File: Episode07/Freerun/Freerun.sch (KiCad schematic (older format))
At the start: 17 parts, among them SW1 SW_Push, U1 MAX708, U2 HD6809, Y1 Crystal

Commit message: minor clarification
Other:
- note added: "You can omit the LED and resistor. I add it as\na power indicator, and also a reset indicator\n(the LED turns off when reset is asserted.)\nUsing a high-efficiency LED and limiting the\ncurrent to a few mA is a good idea."
- note removed: "You can omit the LED and resistor. I add it as\na power indicator, and also a reset indicator\n(the LED turns off when reset is asserted.)"
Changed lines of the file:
@@
 Crystal frequency should be between 2 and 4 MHz.\nI used 3.8668 MHz.
 Text Notes 5300 1350 0    50   ~ 0
-You can omit the LED and resistor.  I add it as\na power indicator, and also a reset indicator\n(the LED turns off when reset is asserted.)
+You can omit the LED and resistor.  I add it as\na power indicator, and also a reset indicator\n(the LED turns off when reset is asserted.)\nUsing a high-efficiency LED and limiting the\ncurrent to a few mA is a good idea.
 Text Notes 6400 6950 0    50   ~ 0
 6809 freerun circuit

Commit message: minor fixes
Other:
- note added: "Crystal frequency should be between 2 and 4 MHz.\nI used 3.6864 MHz."
- note removed: "Crystal frequency should be between 2 and 4 MHz.\nI used 3.8668 MHz."
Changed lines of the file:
@@
 EESchema Schematic File Version 4
+LIBS:Freerun-cache
 EELAYER 26 0
 EELAYER END
@@
 	1    0    0    -1
 $EndComp
-Text Notes 6800 6350 0    50   ~ 0
+Text Notes 6800 6600 0    50   ~ 0
 Make all of the pull-up/pull-down resistors connected\nto the data bus (D0..D7) fairly large, e.g., 4.7K.  The\nresistors cause the CPU to read the value 0x12 when\nan instruction is fetched.  0x12 is the opcode of the\nNOP instruction.
 Wire Wire Line
@@
 	3000 3650 3000 3350
 Text Notes 5500 2900 0    50   ~ 0
-Crystal frequency should be between 2 and 4 MHz.\nI used 3.8668 MHz.
+Crystal frequency should be between 2 and 4 MHz.\nI used 3.6864 MHz.
 Text Notes 5300 1350 0    50   ~ 0
 You can omit the LED and resistor.  I add it as\na power indicator, and also a reset indicator\n(the LED turns off when reset is asserted.)\nUsing a high-efficiency LED and limiting the\ncurrent to a few mA is a good idea.

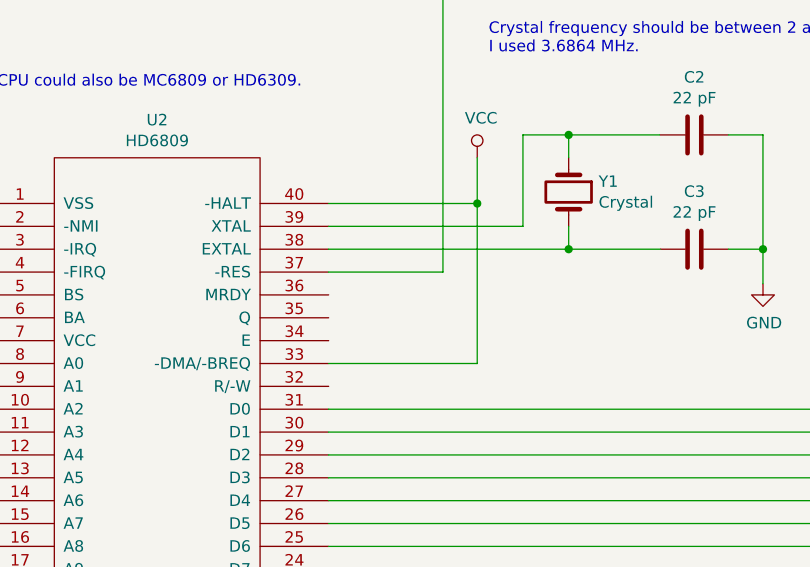
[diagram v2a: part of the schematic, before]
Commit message: connect MRDY input to VCC
With this fix the circuit appears to work (expected
frequencies are observed on A0..A15)
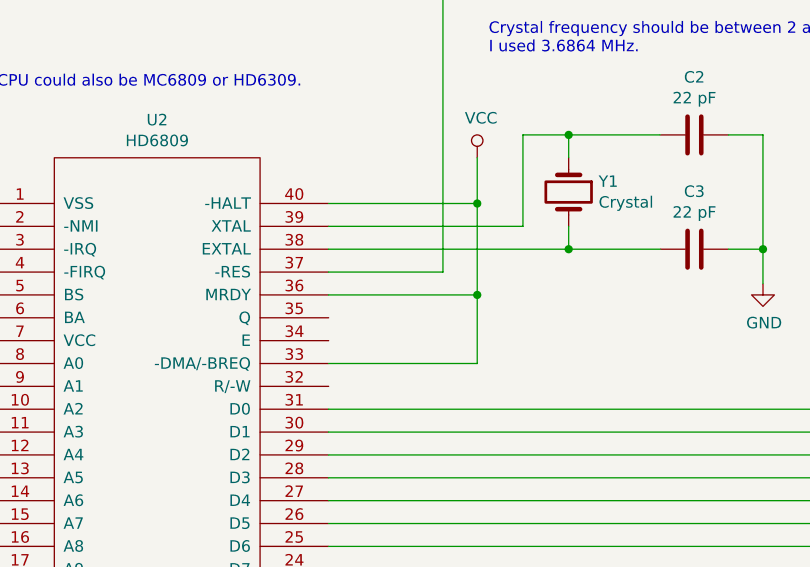
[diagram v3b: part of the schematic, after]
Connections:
- net VCC: now also U2.36 (MRDY)
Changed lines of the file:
@@
 	4800 4250 5450 4250
 Wire Wire Line
-	5450 4250 5450 3550
+	5450 4250 5450 3950
 Connection ~ 5450 3550
 $Comp
@@
 Text Notes 3350 3050 0    50   ~ 0
 CPU could also be MC6809 or HD6309.
+Wire Wire Line
+	4800 3950 5450 3950
+Connection ~ 5450 3950
+Wire Wire Line
+	5450 3950 5450 3550
 $EndSCHEMATC
